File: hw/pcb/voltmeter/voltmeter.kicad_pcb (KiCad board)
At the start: 2 copper layers, 32 parts, among them J0 1935161, Q1 2N7002, Q2 2N7002, U1 SN74HC595DR, U2 TL062

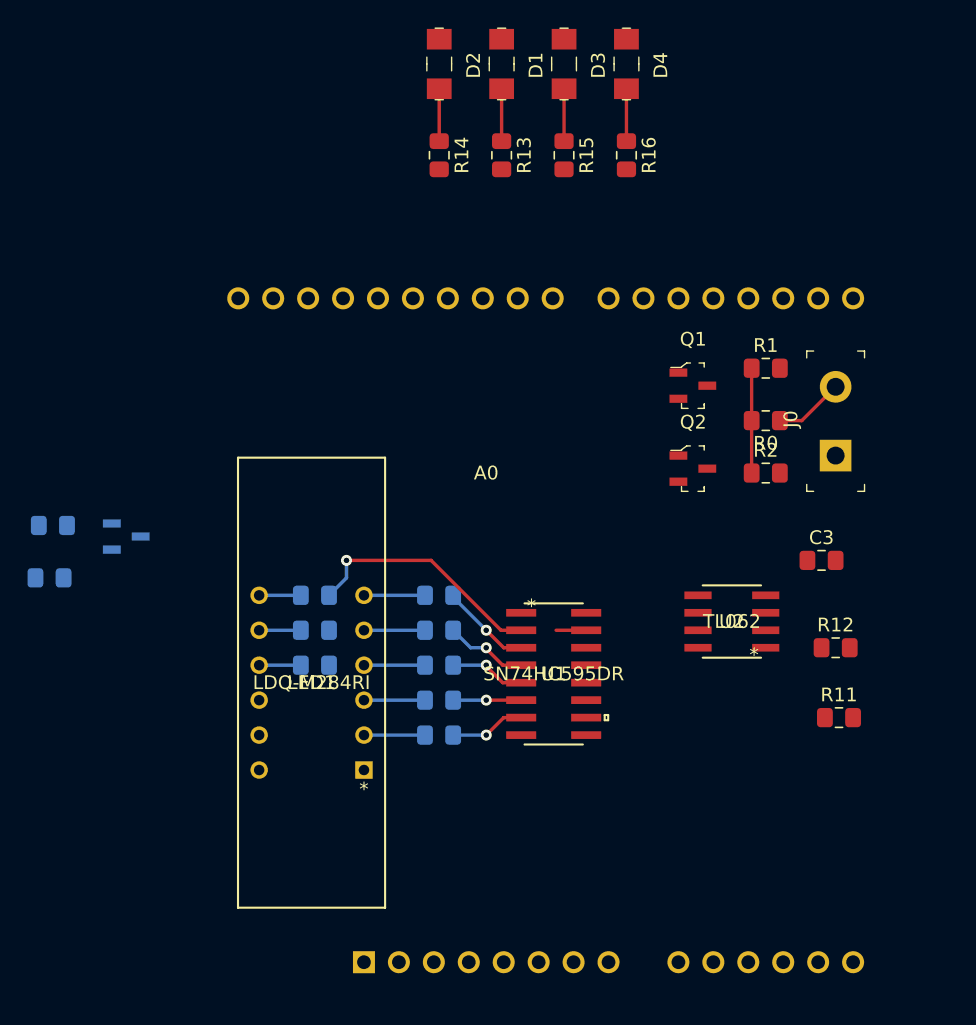
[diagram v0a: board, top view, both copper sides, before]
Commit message: Layout update.
All components on the board. Saving a layout checkpoint for experimenting things.
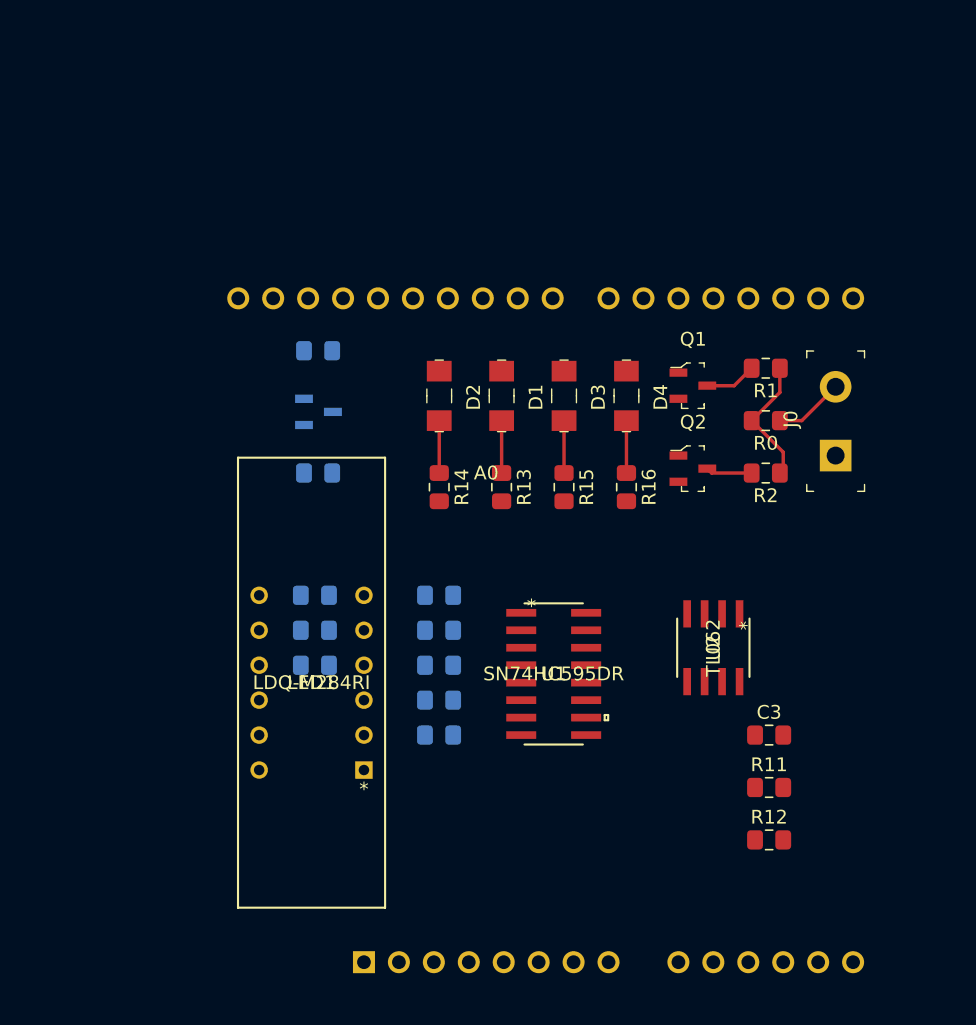
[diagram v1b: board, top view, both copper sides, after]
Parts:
- moved D1 24.1 mm to (135.7, 87.1)
- moved D2 24.1 mm to (131.2, 87.1)
- moved D3 24.1 mm to (140.3, 87.1)
- moved D4 24.1 mm to (144.8, 87.1)
- moved R13 24.1 mm to (135.7, 93.7)
- moved R14 24.1 mm to (131.2, 93.7)
- moved R15 24.1 mm to (140.3, 93.7)
- moved R16 24.1 mm to (144.8, 93.7)
- moved C2 23.1 mm to (122.4, 83.8)
- moved C1 21.0 mm to (122.4, 92.7), turned to 0 degrees
- moved VR1 16.7 mm to (122.4, 88.3)
- moved R12 14.8 mm to (155.2, 119.4)
- moved C3 13.3 mm to (155.2, 111.8)
- moved R11 7.18 mm to (155.2, 115.6)
- moved U2 2.33 mm to (151.1, 105.4), turned to 270 degrees
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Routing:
- net Net-(R8-Pad2): track 17.9 -> 0.00 mm, vias 1 -> 0
- net Net-(R7-Pad2): track 6.60 -> 0.14 mm, vias 1 -> 0
- net Net-(R6-Pad2): track 6.04 -> 0.00 mm, vias 1 -> 0
- net Net-(R5-Pad2): track 5.51 -> 0.00 mm, vias 1 -> 0
- net Net-(R3-Pad2): track 5.47 -> 0.00 mm, vias 1 -> 0
- net Net-(R4-Pad2): track 4.94 -> 0.00 mm, vias 1 -> 0
- net Net-(LED1-Pad6): track 4.43 -> 0.00 mm
- net Net-(LED1-Pad5): track 4.43 -> 0.00 mm
- net Net-(LED1-Pad4): track 4.43 -> 0.00 mm
- net Net-(LED1-Pad3): track 4.43 -> 0.00 mm
- net Net-(LED1-Pad2): track 4.43 -> 0.00 mm
- net Net-(Q1-Pad3): track 0.00 -> 3.75 mm
- net Net-(Q2-Pad3): track 0.00 -> 3.36 mm
- net Net-(LED1-Pad9): track 3.03 -> 0.00 mm
- net Net-(LED1-Pad8): track 3.03 -> 0.00 mm
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
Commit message: Finished the layout!
Committing finalized layout.
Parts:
- C1, C2, R10, R3, R4, R5, R6, R7, R8, R9, VR1: moved to F.Cu
- moved R8 43.0 mm to (165.1, 99.3), turned to 270 degrees
- moved J0 42.1 mm to (118.1, 95.2)
- moved R9 40.5 mm to (162.4, 99.3), turned to 270 degrees
- moved R10 38.2 mm to (159.7, 99.3), turned to 270 degrees
- moved C1 34.1 mm to (137.6, 123.2), turned to 180 degrees
- moved C2 34.1 mm to (137.6, 114.3), turned to 180 degrees
- moved VR1 34.1 mm to (137.7, 118.7), turned to 180 degrees
- moved R1 33.0 mm to (123.2, 94.0), turned to 0 degrees
- moved R2 32.4 mm to (123.2, 86.4), turned to 0 degrees
- moved R0 31.8 mm to (123.2, 90.2), turned to 0 degrees
- moved D4 31.0 mm to (130.1, 114.3), turned to 180 degrees
- moved R16 29.7 mm to (123.4, 114.3), turned to 180 degrees
- moved LED1 27.0 mm to (143.5, 94.0), turned to 90 degrees
- moved R7 25.8 mm to (156.9, 99.3), turned to 270 degrees
- moved D3 24.9 mm to (130.1, 109.8), turned to 180 degrees
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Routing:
- net /VoltageDivider: track 9.52 -> 71.2 mm, vias 0 -> 2
- net 1.2vLeg: track 0.00 -> 55.6 mm, vias 0 -> 3
- net VCC: track 0.00 -> 53.8 mm, vias 0 -> 2
- net Net-(A0-Pad26): track 0.00 -> 51.7 mm, vias 0 -> 3
- net 15vLeg: track 0.00 -> 50.9 mm, vias 0 -> 3
- net AREF_4.096v: track 0.00 -> 49.2 mm, vias 0 -> 1
- net Net-(A0-Pad28): track 0.00 -> 48.9 mm, vias 0 -> 4
- net 5vLeg: track 0.00 -> 47.9 mm, vias 0 -> 3
- net Net-(A0-Pad25): track 0.00 -> 47.5 mm, vias 0 -> 3
- net 30vLeg: track 0.00 -> 43.0 mm, vias 0 -> 3
- net ADC-Unity: track 0.00 -> 34.6 mm, vias 0 -> 1
- net ADC-Gain: track 0.00 -> 25.4 mm
- net Net-(R10-Pad2): track 0.00 -> 17.4 mm, vias 0 -> 2
- net Net-(A0-Pad19): track 0.00 -> 17.1 mm
- net Net-(LED1-Pad9): track 0.00 -> 16.2 mm
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- added copper zone on B.Cu, net GND
- added copper zone on F.Cu, net GND
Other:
- board outline added: 53.3 x 53.3 mm
- rule trace_min: 0.2 -> 0.1524
- rule via_min_size: 0.4 -> 0.1524

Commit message: Generated gerber files.
Generated gerber files. Beginning final component checks.
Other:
- rule pad_to_mask_clearance: 0.05 -> 0.0508
- board text added: "AMW NRR MMA"
- board text added: "Blue Smoke Generator"
- board text added: "https://github.com/markmatthewanderson/voltmeter_shield"

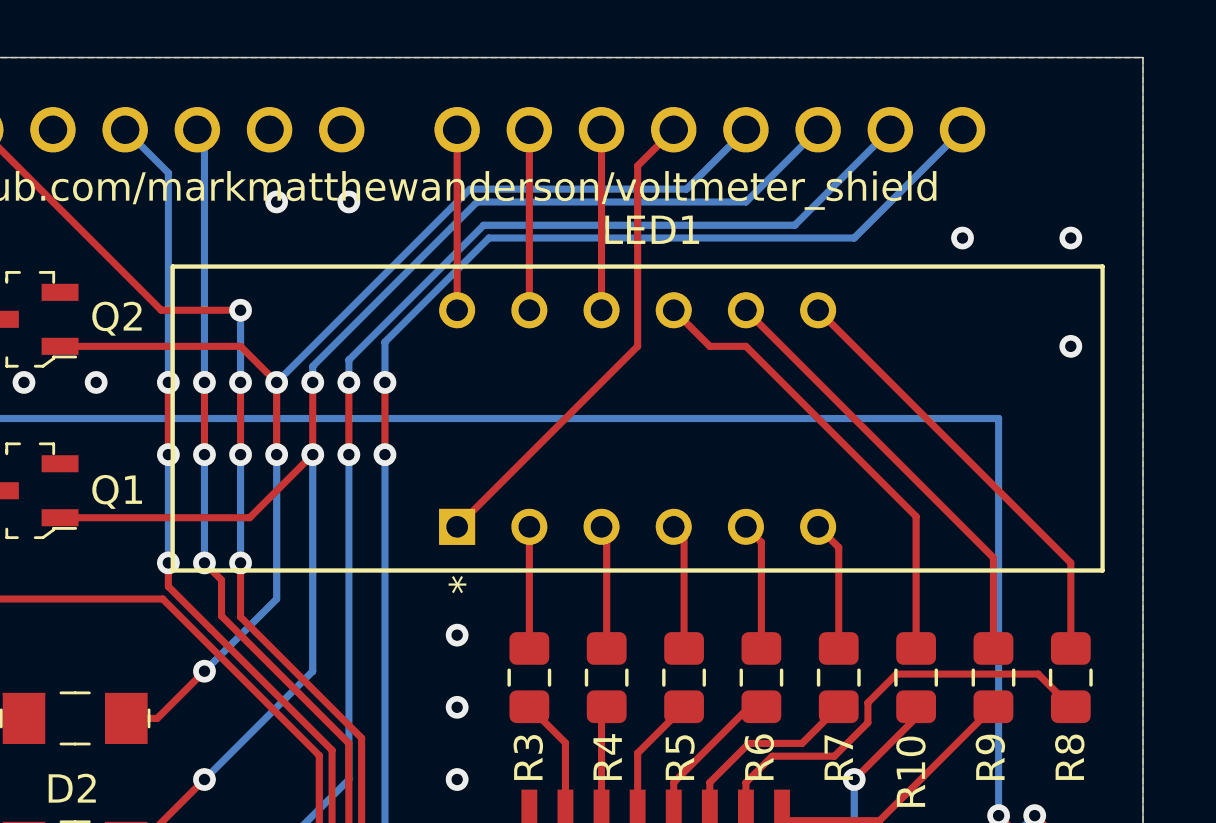
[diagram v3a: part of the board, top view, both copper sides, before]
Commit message: Fix incorrect 7-segment pinout.
Fixed bad 7-segment pinout. Fixed layout; regenerated gerbers.
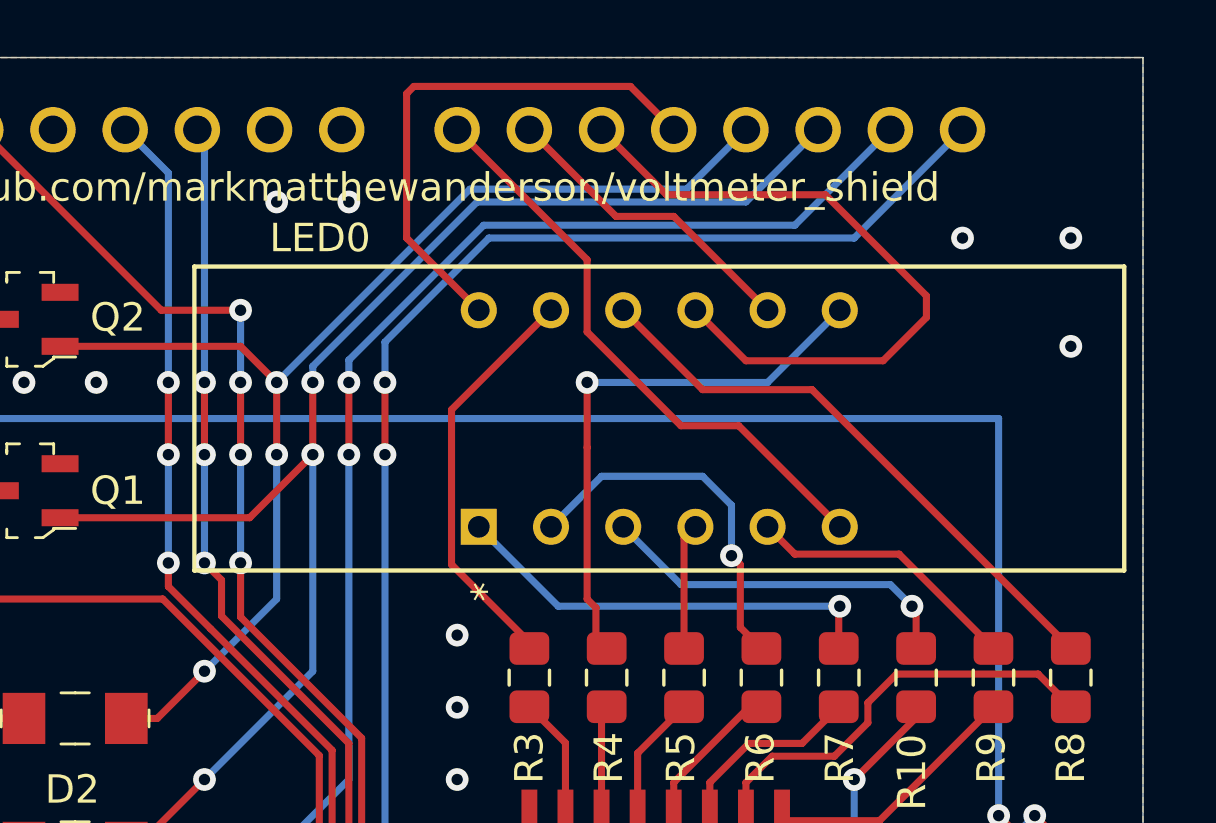
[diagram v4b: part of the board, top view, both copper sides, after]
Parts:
- removed LED1: LDQ-M284RI, footprints3:LDQ-M284RI
- added LED0: LDQ-M284RI, footprints4:LDQ-M284RI, F.Cu at (144.3, 94.0)
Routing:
- net Net-(A0-Pad20): track 6.35 -> 24.1 mm
- net Net-(LED0-Pad7): track 4.36 -> 19.6 mm, vias 0 -> 1
- net Net-(A0-Pad22): track 6.35 -> 20.7 mm
- net Net-(LED0-Pad1): track 4.58 -> 15.4 mm, vias 0 -> 1
- net Net-(LED0-Pad11): track 4.28 -> 14.5 mm
- net Net-(LED0-Pad2): track 4.51 -> 13.0 mm, vias 0 -> 1
- net Net-(LED0-Pad5): track 15.5 -> 9.72 mm
- net Net-(LED0-Pad10): track 15.6 -> 20.7 mm
- net Net-(A0-Pad21): track 6.35 -> 11.0 mm
- net Net-(LED0-Pad3): track 16.2 -> 12.9 mm, vias 0 -> 1
- net Net-(A0-Pad19): track 17.1 -> 18.8 mm

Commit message: Added voltage scale labels to LEDs.
Added voltage scale labels to LEDs. Regenerated gerber files.
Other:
- board text added: "1.2V Scale"
- board text added: "15V Scale"
- board text added: "30V Scale"
- board text added: "5V Scale"

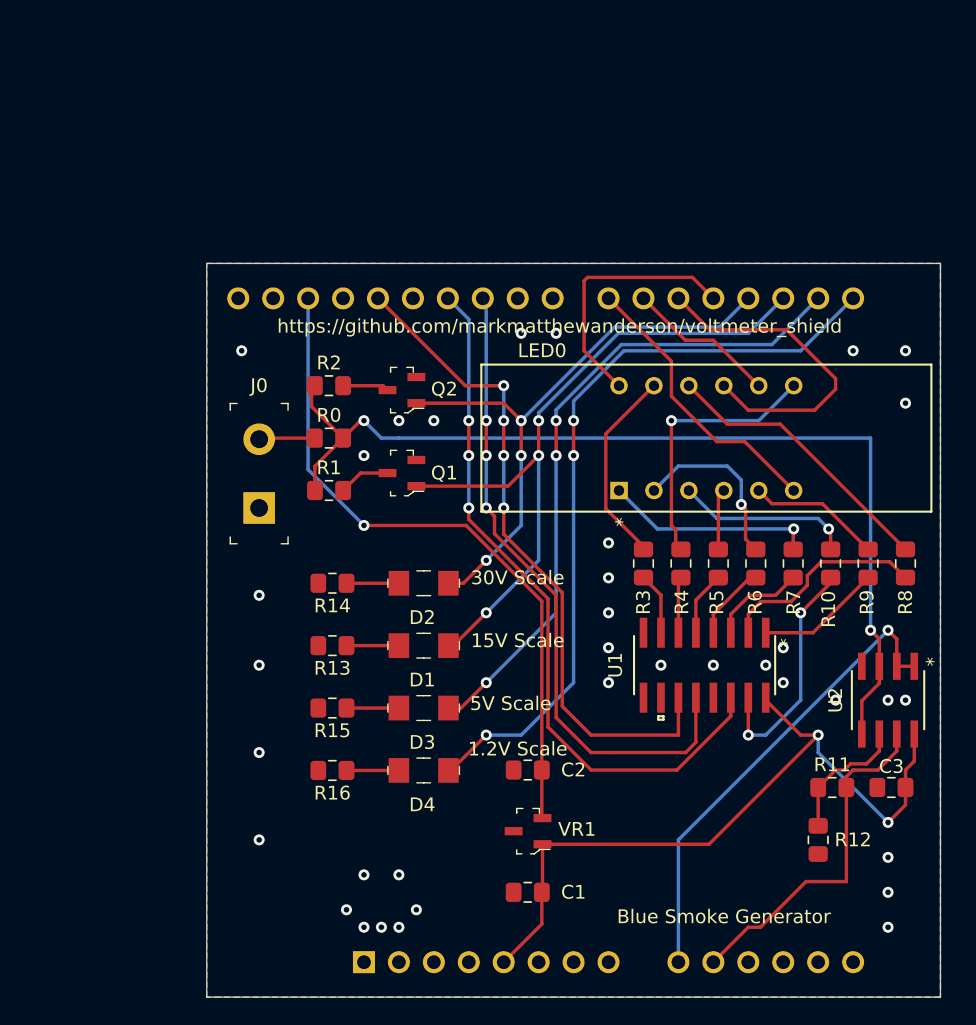
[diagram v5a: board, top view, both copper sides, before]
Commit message: Finalize board for order.
Finalized BOM, saved BOM from DigiKey.
Updated layout to match updated BOM.
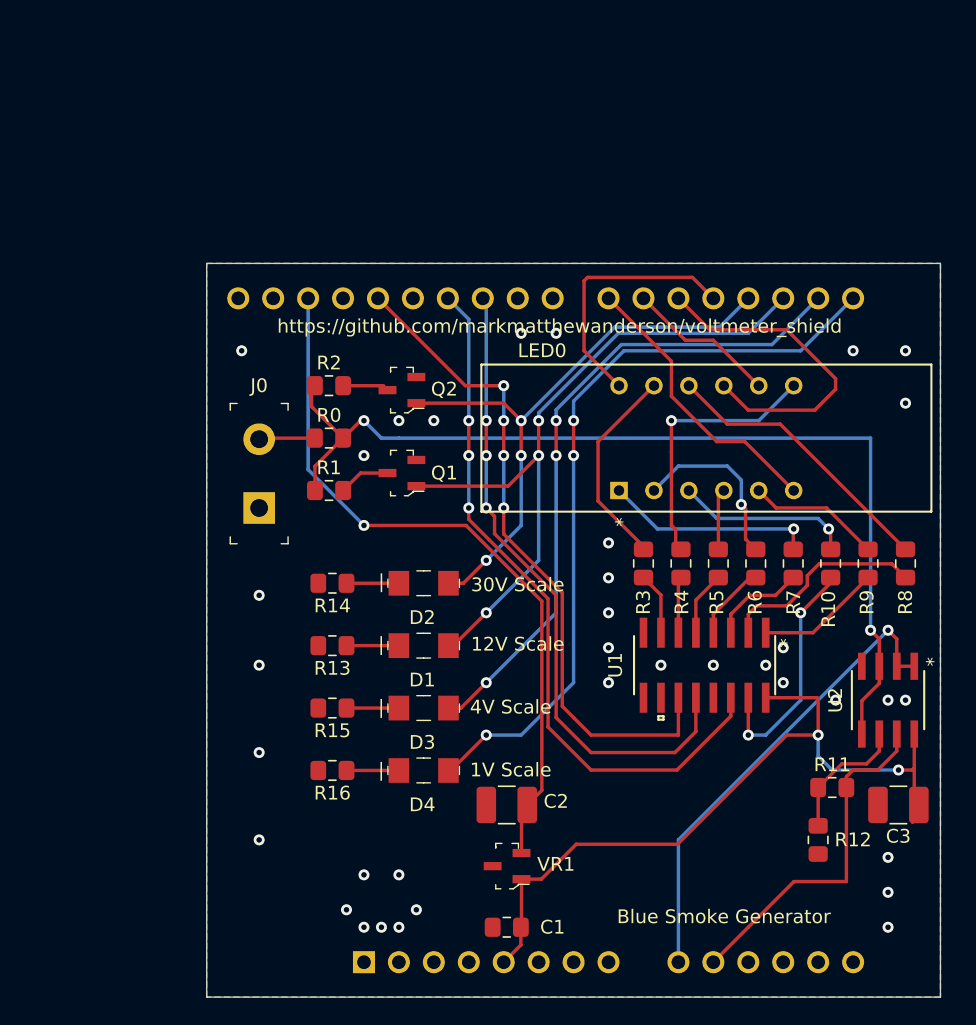
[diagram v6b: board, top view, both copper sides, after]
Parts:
- C2, C3: footprint Capacitor_SMD:C_0805_2012Metric_Pad1.15x1.40mm_HandSolder -> Capacitor_SMD:C_1210_3225Metric_Pad1.42x2.65mm_HandSolder
- U2: value TL062 -> TL062CDR
- moved C1 2.96 mm to (136.1, 125.7)
- moved C2 2.96 mm to (136.1, 116.8)
- moved VR1 2.96 mm to (136.1, 121.3)
- moved C3 1.37 mm to (164.6, 116.8)
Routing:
- net AREF_4.096v: track 49.2 -> 52.4 mm
- net VCC: track 53.8 -> 54.7 mm
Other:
- board text added: "12V Scale"
- board text added: "1V Scale"
- board text added: "4V Scale"
- board text added: "|"
- board text removed: "1.2V Scale"
- board text removed: "15V Scale"
- board text removed: "5V Scale"

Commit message: Schematic fix & updated Arduino pins.
Fixed active low SRCLR pin on 595 shift register. Added test Arduino code. Fixed Arduino code pins.
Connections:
- U1 pad 10: GND -> VCC
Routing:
- net VCC: track 54.7 -> 65.3 mm
- net Net-(A0-Pad26): track 51.7 -> 52.8 mm
- net GND: vias 36 -> 34
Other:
- board text added: "Rev. 2"
